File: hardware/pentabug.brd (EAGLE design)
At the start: 33 x 100 mm, 15 parts, among them IC1 ATMEGA88

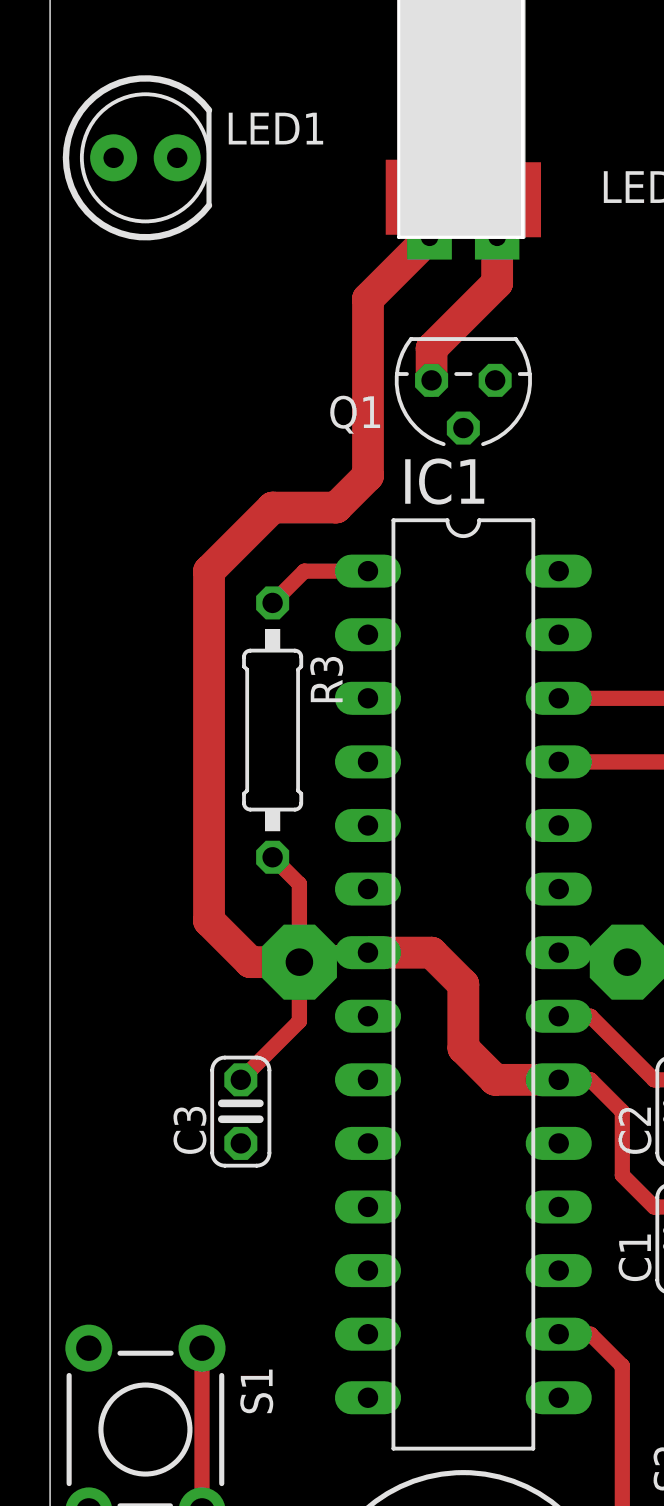
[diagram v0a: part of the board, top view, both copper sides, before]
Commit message: some more routing, added new buzzr footprint
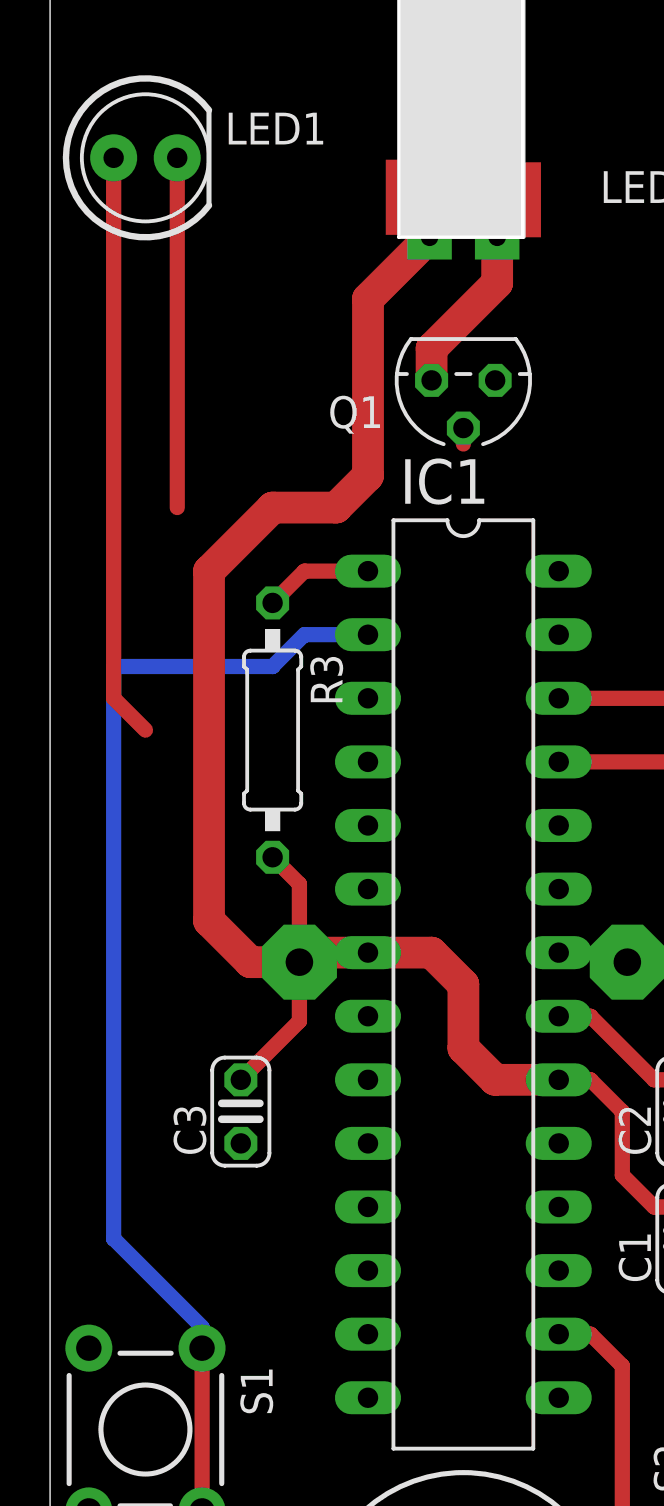
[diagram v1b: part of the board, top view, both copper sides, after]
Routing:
- net RX: track 21.6 -> 61.0 mm
- net N$3: track 0.00 -> 23.4 mm
- net N$10: track 0.00 -> 14.0 mm
- net VIBRATE: track 0.00 -> 0.63 mm
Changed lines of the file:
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@@
 <wire x1="9.96" y1="53.54" x2="9.96" y2="50.42" width="0.6096" layer="1"/>
 <wire x1="9.96" y1="50.42" x2="10.34" y2="50.8" width="0.6096" layer="1"/>
-<wire x1="10.34" y1="50.8" x2="12.7" y2="50.8" width="0.6096" layer="1"/>
+<wire x1="10.34" y1="50.8" x2="12.7" y2="50.8" width="1.27" layer="1"/>
 <wire x1="9.96" y1="50.42" x2="8" y2="50.42" width="1.27" layer="1"/>
 <wire x1="8" y1="50.42" x2="6.35" y2="52.07" width="1.27" layer="1"/>
@@
 <contactref element="JP1" pad="2"/>
 <wire x1="26.9494" y1="35.0012" x2="26.9494" y2="28.4988" width="0.6096" layer="1"/>
-<wire x1="26.9494" y1="35.0012" x2="12.7" y2="60.96" width="0" layer="19" extent="1-1"/>
 <wire x1="5.877" y1="16.25" x2="5.877" y2="16.037" width="0.6096" layer="1"/>
 <wire x1="5.877" y1="16.037" x2="3.81" y2="13.97" width="0.6096" layer="1"/>
@@
 <wire x1="19.05" y1="20.32" x2="26.9494" y2="28.2194" width="0.6096" layer="1"/>
 <wire x1="26.9494" y1="28.2194" x2="26.9494" y2="28.4988" width="0.6096" layer="1"/>
+<wire x1="26.9494" y1="35.0012" x2="12.7" y2="60.96" width="0" layer="19" extent="1-1"/>
 </signal>
 <signal name="RX">
@@
 <wire x1="1.27" y1="24.13" x2="1.27" y2="20.856996875" width="0.6096" layer="1"/>
 <wire x1="1.27" y1="20.856996875" x2="4.080946875" y2="18.04605" width="0.6096" layer="1"/>
-<wire x1="6.0706" y1="35.0012" x2="12.7" y2="63.5" width="0" layer="19" extent="1-1"/>
+<wire x1="12.7" y1="63.5" x2="10.16" y2="63.5" width="0.6096" layer="16"/>
+<wire x1="10.16" y1="63.5" x2="8.89" y2="62.23" width="0.6096" layer="16"/>
+<wire x1="8.89" y1="62.23" x2="2.54" y2="62.23" width="0.6096" layer="16"/>
+<wire x1="2.54" y1="62.23" x2="2.54" y2="39.37" width="0.6096" layer="16"/>
+<wire x1="2.54" y1="39.37" x2="6.0706" y2="35.8394" width="0.6096" layer="16"/>
+<wire x1="6.0706" y1="35.8394" x2="6.0706" y2="35.0012" width="0.6096" layer="16"/>
 </signal>
 <signal name="N$3">
 <contactref element="IC1" pad="23"/>
 <contactref element="LED1" pad="A"/>
-<wire x1="20.32" y1="53.34" x2="2.54" y2="82.55" width="0" layer="19" extent="1-1"/>
+<wire x1="2.54" y1="82.55" x2="2.54" y2="60.96" width="0.6096" layer="1"/>
+<wire x1="2.54" y1="60.96" x2="3.81" y2="59.69" width="0.6096" layer="1"/>
+<wire x1="3.81" y1="59.69" x2="20.32" y2="53.34" width="0" layer="19" extent="1-16"/>
 </signal>
 <signal name="N$5">
@@
 <contactref element="LED1" pad="K"/>
 <contactref element="IC1" pad="24"/>
-<wire x1="20.32" y1="55.88" x2="5.08" y2="82.55" width="0" layer="19" extent="1-1"/>
+<wire x1="5.08" y1="82.55" x2="5.08" y2="68.58" width="0.6096" layer="1"/>
+<wire x1="5.08" y1="68.58" x2="20.32" y2="55.88" width="0" layer="19" extent="1-16"/>
 </signal>
 <signal name="N$11">
@@
 <contactref element="IC1" pad="15"/>
 <contactref element="Q1" pad="2"/>
-<wire x1="20.32" y1="33.02" x2="16.51" y2="71.755" width="0" layer="19" extent="1-1"/>
+<wire x1="16.51" y1="71.755" x2="16.51" y2="71.12" width="0.6096" layer="1"/>
+<wire x1="16.51" y1="71.12" x2="20.32" y2="33.02" width="0" layer="19" extent="1-16"/>
 </signal>
 <signal name="N$8">
@@
 <wire x1="3.81" y1="8.89" x2="1.27" y2="11.43" width="0.6096" layer="1"/>
 <wire x1="1.27" y1="11.43" x2="1.27" y2="15.24" width="0.6096" layer="1"/>
-<wire x1="1.27" y1="15.24" x2="8.89" y2="64.77" width="0" layer="19" extent="1-16"/>
+<wire x1="1.27" y1="15.24" x2="8.89" y2="64.77" width="0" layer="19" extent="1-1"/>
 </signal>
 <signal name="MOSI">

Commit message: some routing
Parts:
- removed SG2: BUZZERPTH, SparkFun:BUZZER-12MM
- added SG1: MULTIBUZZR, buglbr:MULTIBUZZR
- moved S2 0.64 mm to (28.6, 31.8)
- moved S1 0.64 mm to (4.45, 31.8)
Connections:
- net BUZZR: now also SG1.+, SG1.+1; no longer SG2.+
- net GND: now also SG1.-, SG1.-1; no longer SG2.-
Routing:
- net TX: track 47.3 -> 100.3 mm
- net N$10: track 14.0 -> 57.0 mm, vias 0 -> 2
- net VIBRATE: track 0.63 -> 41.8 mm
- net N$3: track 23.4 -> 63.9 mm, vias 0 -> 2
- net RX: track 61.0 -> 53.4 mm
- net BUZZR: track 14.5 -> 10.1 mm
- net N$5: track 32.8 -> 30.6 mm
- net N$11: track 28.5 -> 26.2 mm
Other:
- board size 33 x 100 mm -> 33 x 89.2 mm

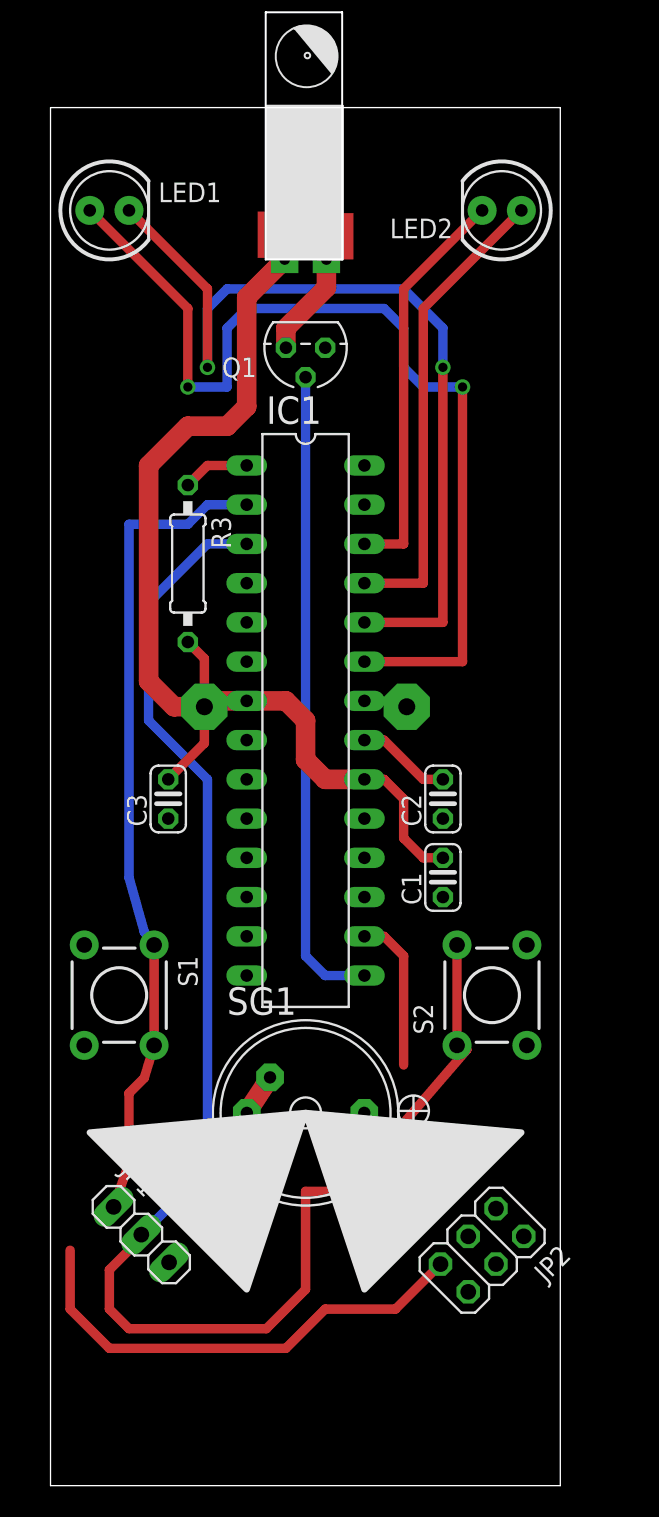
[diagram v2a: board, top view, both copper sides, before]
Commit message: Lots of routing done, GND from Buzzer connected to ADC6 for measurement
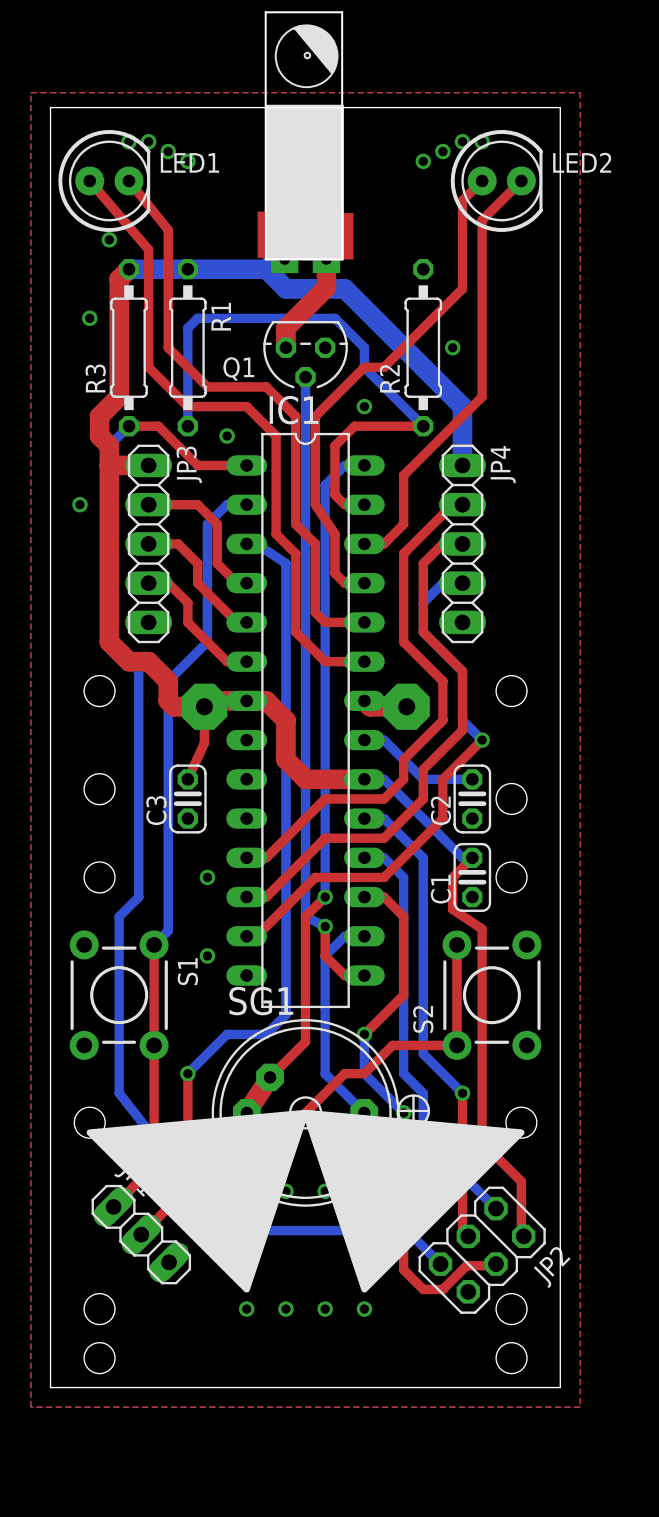
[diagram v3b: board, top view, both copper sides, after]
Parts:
- added JP3, JP4: (no value), pinhead:1X05
- added R1: 100K, rcl:0207/10
- added R2: 18K, rcl:0207/10
- moved R3 14.5 mm to (5.08, 73.7), turned to 90 degrees
- moved C1 1.91 mm to (27.3, 39.4)
- moved C2 1.91 mm to (27.3, 44.5)
- moved LED1 1.91 mm to (3.81, 84.5)
- moved LED2 1.91 mm to (29.2, 84.5), turned to 0 degrees
- moved C3 1.27 mm to (8.89, 44.5)
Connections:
- net N$11 renamed BATTLVL
- removed net N$22: IC1.6
- removed net N$4: IC1.4
- removed net N$7: IC1.11
- removed net N$9: IC1.5
- new net BATLVL: IC1.27, R1.2, R2.1
- new net BUZGND: IC1.28, SG1.-, SG1.-1
- new net PD2: IC1.4, JP3.2
- new net PD3: IC1.5, JP3.3
- new net PD4: IC1.6, JP3.4
- new net PD5: IC1.11, JP4.2
- new net PD7: IC1.13, JP4.4
- net GND: now also JP3.5, JP4.5, R2.2; no longer SG1.-, SG1.-1
- net PD6: now also JP4.3
- net VCC: now also JP2.2, JP3.1, JP4.1, R1.1
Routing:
- net VCC: track 69.8 -> 122.2 mm
- net RST: track 35.4 -> 79.7 mm
- net BUZGND: track 0.00 -> 42.9 mm, vias 0 -> 1
- net BATLVL: track 0.00 -> 37.1 mm
- net PD7: track 0.00 -> 35.5 mm, vias 0 -> 1
- net MOSI: track 0.00 -> 35.2 mm, vias 0 -> 2
- net PD6: track 0.00 -> 34.5 mm
- net PD5: track 0.00 -> 34.1 mm
- net SCK: track 0.00 -> 30.6 mm, vias 0 -> 1
- net MISO: track 0.00 -> 27.0 mm
- net TX: track 100.3 -> 78.7 mm, vias 0 -> 1
- net N$3: track 63.9 -> 43.3 mm, vias 2 -> 0
- net N$10: track 57.0 -> 38.4 mm, vias 2 -> 0
- net PD2: track 0.00 -> 9.94 mm
- net PD3: track 0.00 -> 9.20 mm
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- added copper zone on layer 1, net GND
- added copper zone on layer 16, net GND
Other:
- board size 33 x 89.2 mm -> 33 x 82.9 mm

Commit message: some routin
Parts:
- moved R1 8.52 mm to (16.5, 69.8), turned to 0 degrees
- moved R2 3.81 mm to (27.9, 73.7)
- moved Q1 0.64 mm to (16.5, 74.3)
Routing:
- net BATLVL: track 37.1 -> 15.9 mm
- net VCC: track 122.2 -> 135.8 mm
- net N$5: track 33.2 -> 32.4 mm
- net VIBRATE: track 41.3 -> 42.0 mm
- net N$8: track 6.80 -> 6.17 mm
- net GND: vias 22 -> 21

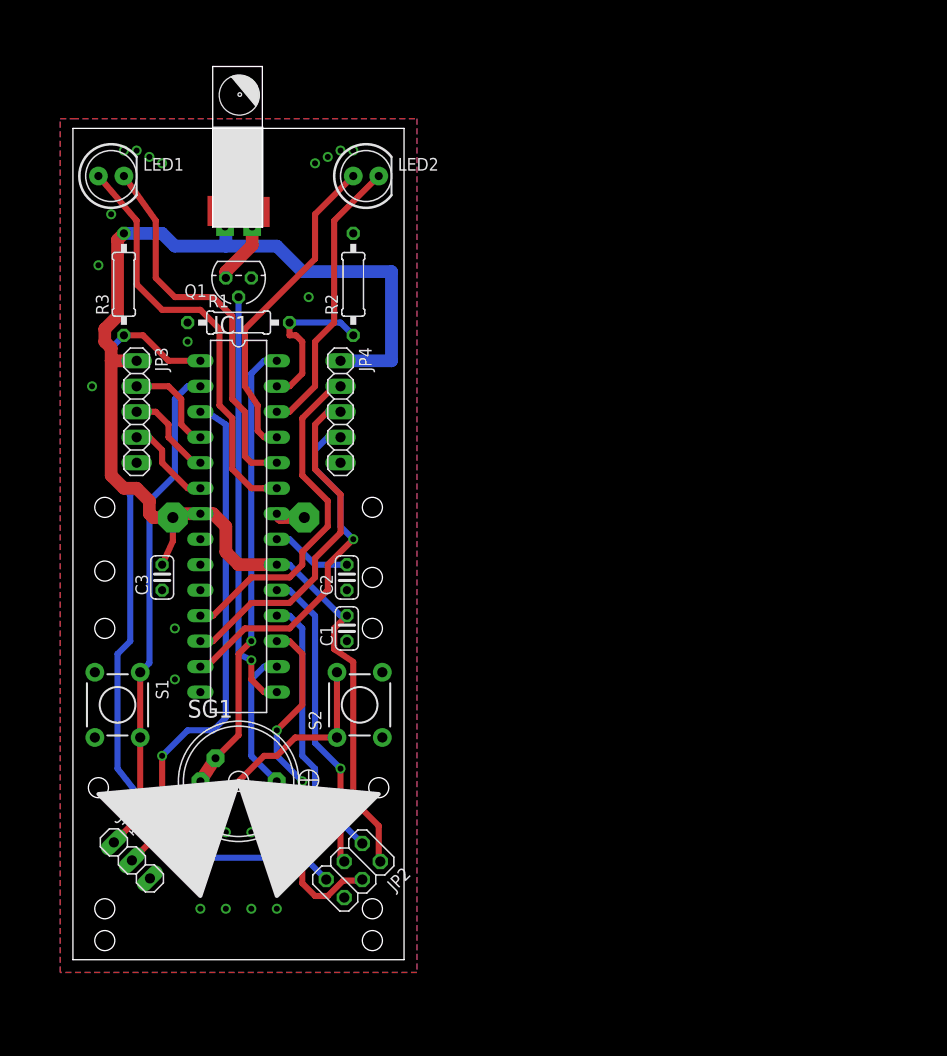
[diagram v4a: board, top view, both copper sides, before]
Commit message: modified to use biggr buzzr - routing not adapted yet!
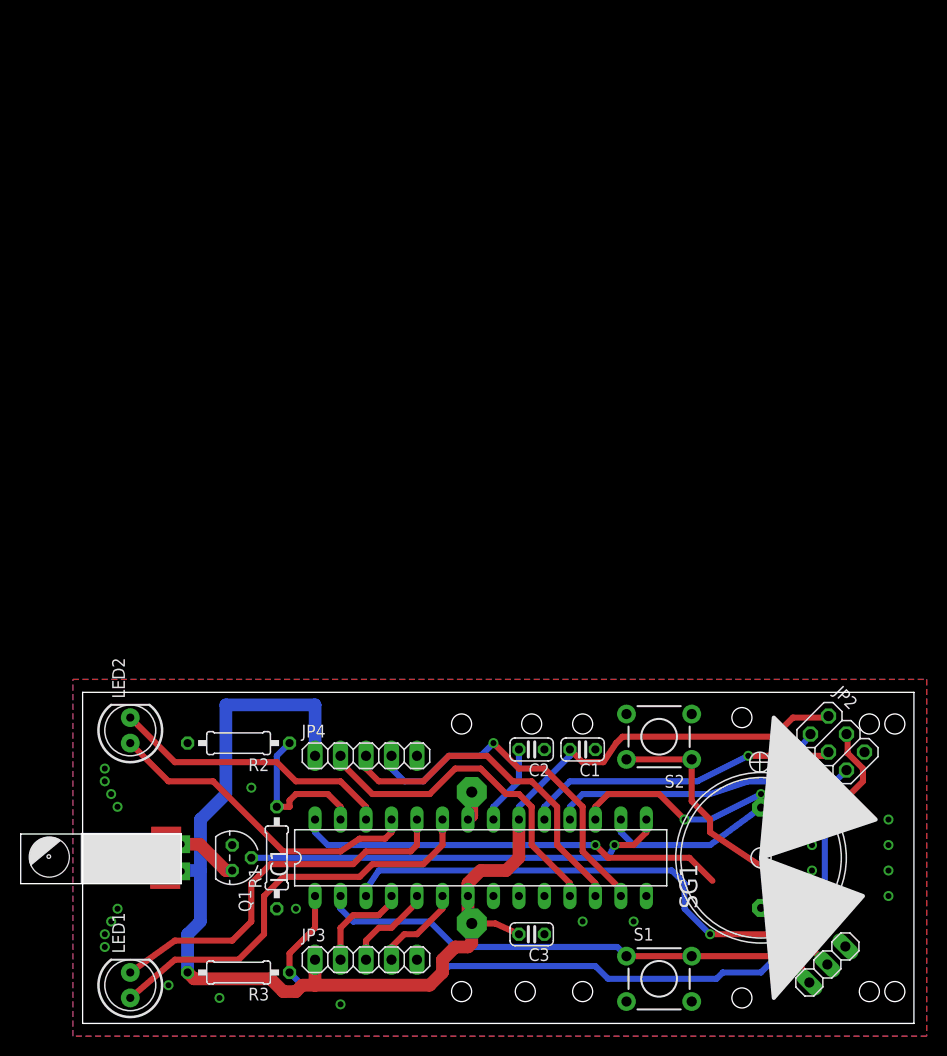
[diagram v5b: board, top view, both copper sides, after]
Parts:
- SG1: value MULTIBUZZR -> MULTIBUZZRTDKBUZZR; device buglbr:MULTIBUZZR -> buglbr:BUZZRTDK
- moved LED1 80.7 mm to (5.71, 3.81), turned to 90 degrees
- moved U$1 71.0 mm to (3.81, 16.5), turned to 180 degrees
- moved JP1 70.1 mm to (75.2, 5.88), turned to 45 degrees
- moved R3 69.5 mm to (16.5, 5.08), turned to 180 degrees
- moved S1 60.5 mm to (58.4, 4.45), turned to 0 degrees
- moved LED2 60.0 mm to (5.71, 29.2), turned to 90 degrees
- moved JP3 59.2 mm to (29.2, 6.35), turned to 0 degrees
- moved Q1 57.8 mm to (15.9, 16.5), turned to 270 degrees
- moved R1 53.5 mm to (20.3, 16.5), turned to 90 degrees
- moved SG1 52.6 mm to (68.6, 16.5), turned to 90 degrees
- moved C3 51.2 mm to (45.7, 8.89), turned to 180 degrees
- moved JP2 49.9 mm to (76.2, 27.9), turned to 315 degrees
- moved BAT1 48.1 mm to (63.5, 16.5), turned to 180 degrees
- moved R2 47.1 mm to (16.5, 27.9), turned to 180 degrees
- moved IC1 40.9 mm to (40.6, 16.5), turned to 0 degrees
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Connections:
- net BUZGND: no longer SG1.-1
- net BUZZR: no longer SG1.+1
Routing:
- net TX: track 78.7 -> 82.0 mm
- net BUZZR: track 14.3 -> 17.0 mm
- net RX: track 49.8 -> 51.5 mm
- net RST: track 79.7 -> 81.5 mm
- net MISO: track 27.0 -> 28.4 mm
- net VCC: track 135.8 -> 137.1 mm
- net MOSI: track 35.2 -> 36.0 mm
- net SCK: track 30.6 -> 31.4 mm
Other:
- board size 33 x 82.9 mm -> 82.9 x 33 mm
